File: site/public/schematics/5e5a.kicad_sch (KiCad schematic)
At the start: 60 parts, among them T2 ~4.3k:8

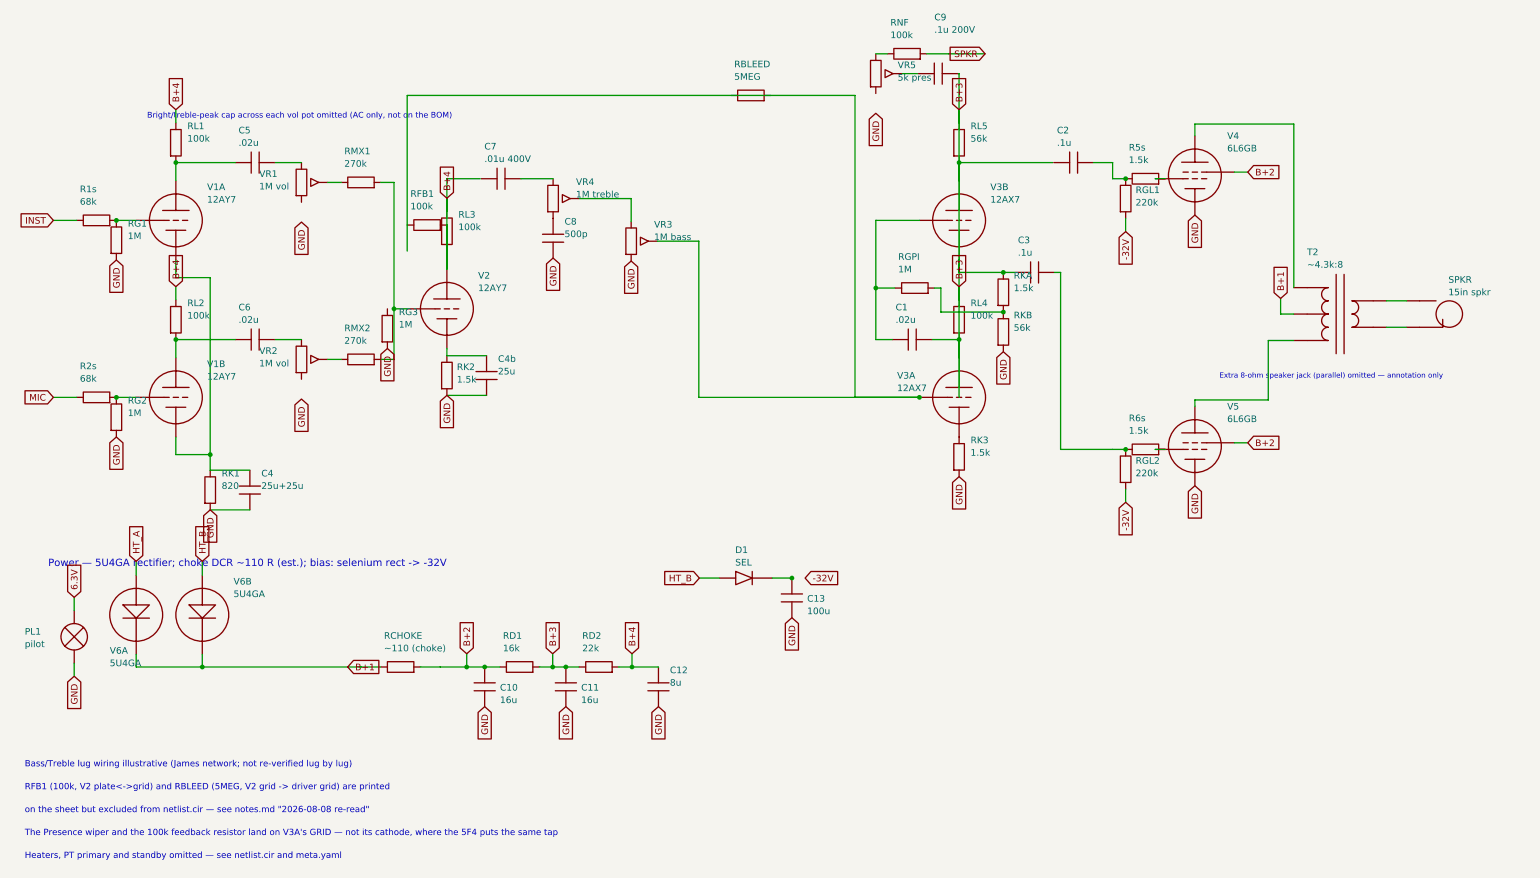
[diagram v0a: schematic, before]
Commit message: Fix: site copies of 29 sheets re-synced; regenerate step syncs before the drift check
- the drawing scripts write amps/; site/public/schematics is refreshed by
  site/scripts/sync-assets.mjs, which CI only ran inside the site build, so
  the fixer commits carried stale copies and the new drift gate caught them
- CI now syncs immediately after regenerating and diffs both trees; the
  AGENTS.md regenerate command does the same

Co-Authored-By: Claude Fable 5.1 <noreply@anthropic.com>
Claude-Session: https://claude.ai/code/session_01KBMfdh37HmCL2iWcBiL5J1
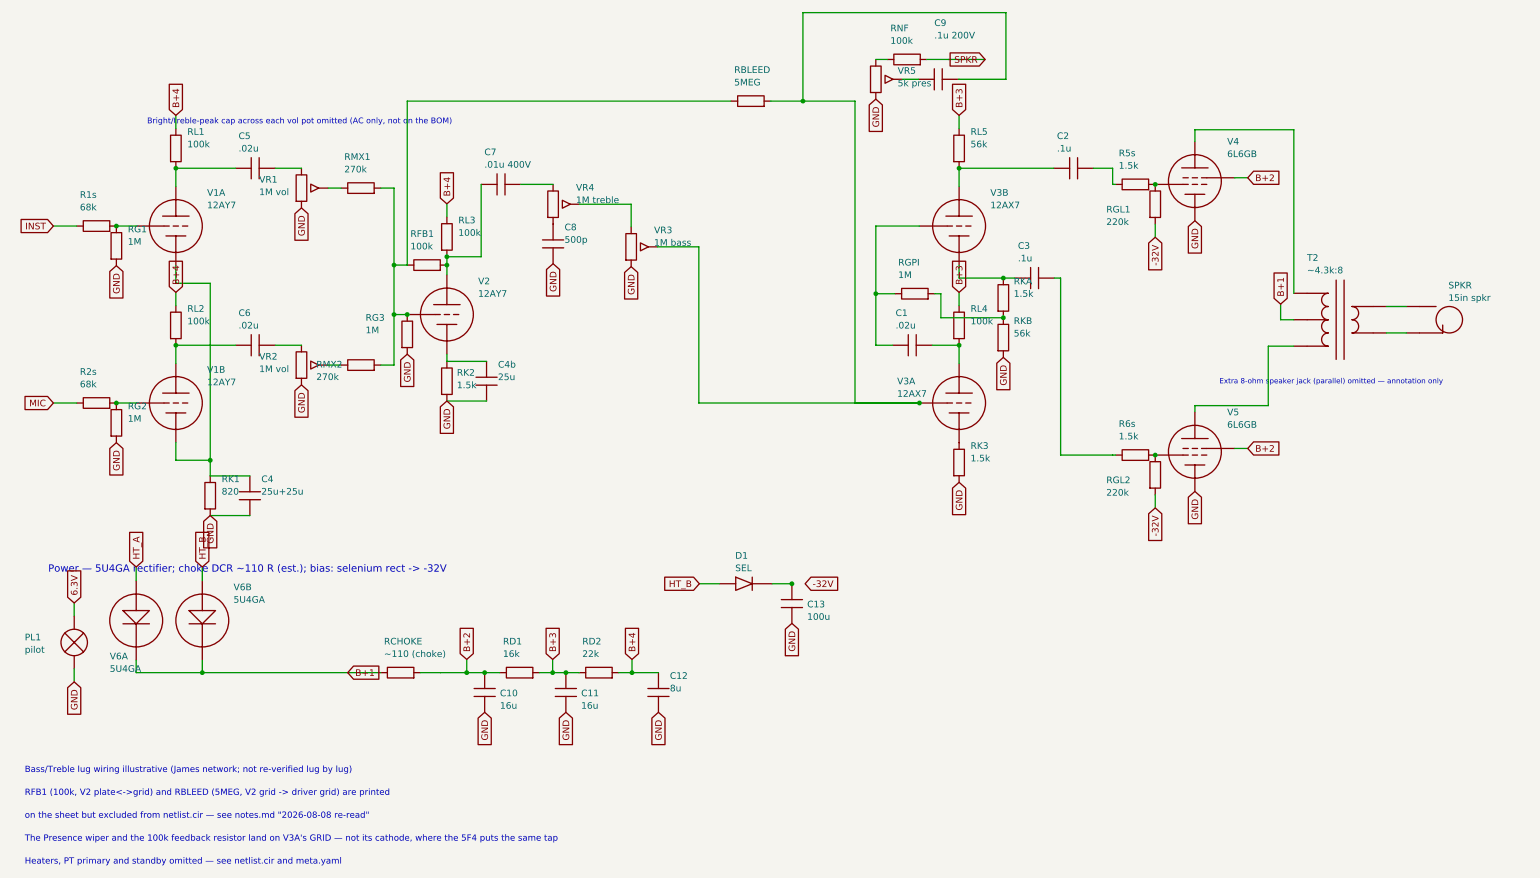
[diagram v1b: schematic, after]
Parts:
- removed C8: 500p, symbol cx:C
- removed RCHOKE: ~110 (choke), symbol cx:R
- removed RGL1, RGL2: 220k, symbol cx:R
- removed RK1: 820, symbol cx:R
- removed RK2, RK3, RKA: 1.5k, symbol cx:R
- removed SPKR: 15in spkr, symbol cx:JACK
- removed V4: 6L6GB, symbol cx:PENTODE
- removed V6B: 5U4GA, symbol cx:DIODE_TUBE
- added C1: .02u, symbol cx:C
- added C2, C3: .1u, symbol cx:C
- added C4: 25u+25u, symbol cx:C
- added C4b: 25u, symbol cx:C
- added PL1: pilot, symbol cx:LAMP
- added RKB: 56k, symbol cx:R
- added T2: ~4.3k:8, symbol cx:OT_PP
- added V3A: 12AX7, symbol cx:TRIODE
- added V6A: 5U4GA, symbol cx:DIODE_TUBE
- added VR4: 1M treble, symbol cx:POT
- C8: renamed from VR4; value 1M treble -> 500p; symbol cx:POT -> cx:C
- RCHOKE: renamed from V6A; value 5U4GA -> ~110 (choke); symbol cx:DIODE_TUBE -> cx:R
- RGL1: renamed from C2; value .1u -> 220k; symbol cx:C -> cx:R
- RGL2: renamed from C3; value .1u -> 220k; symbol cx:C -> cx:R
- RGPI: renamed from C1; value .02u -> 1M; symbol cx:C -> cx:R
- RK1: renamed from C4; value 25u+25u -> 820; symbol cx:C -> cx:R
- RK2: renamed from C4b; value 25u -> 1.5k; symbol cx:C -> cx:R
- RK3: renamed from RL4; value 100k -> 1.5k
- RKA: renamed from RGPI; value 1M -> 1.5k
- RL4: renamed from V3A; value 12AX7 -> 100k; symbol cx:TRIODE -> cx:R
- SPKR: renamed from T2; value ~4.3k:8 -> 15in spkr; symbol cx:OT_PP -> cx:JACK
- V4: renamed from RKB; value 56k -> 6L6GB; symbol cx:R -> cx:PENTODE
- V6B: renamed from PL1; value pilot -> 5U4GA; symbol cx:LAMP -> cx:DIODE_TUBE
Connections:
- net -32V: now also RGL1.2, RGL2.2
- net 6.3V: now also PL1.1; no longer V6B.1
- net B+1: now also RCHOKE.1, V6B.2 (K), T2.2 (CT), V6A.2 (K); no longer RCHOKE.2 (K)
- net B+2: now also RCHOKE.2, V4.3 (G2)
- net B+3: no longer C9.2, RGL2.1, RGPI.2, RK3.1, RK3.2, RL5.2, V3B.1 (P), V3B.3 (K)
- net B+4: no longer RFB1.2, RL3.2, V2.1 (P)
- net GND: now also C8.2, RK3.2, V4.4 (K), VR1.3, VR2.3, VR5.3, C4.2, C4b.2, PL1.2, RKB.2; no longer V4.2, V6B.2
- net HT_A: now also V6A.1 (A); no longer RCHOKE.1 (A)
- net HT_B: now also V6B.1 (A)
- net at C7.1: now also RFB1.2, RL3.2, V2.1 (P)
- net at C7.2: now also VR4.1; no longer C8.1
- net at V4.1 (P): now also T2.1 (PRI_A); no longer RKA.2
- net at RGL1.1: now also R5s.2, V4.2 (G1)
- net at R5s.1: now also C2.2; no longer RGL1.2
- net at V5.1 (P): now also T2.3 (PRI_B)
- net at R6s.2, V5.2 (G1): now also RGL2.1
- net at R6s.1: now also C3.2; no longer RGL2.2
- net at RK2.1, V2.3 (K): now also C4b.1
- net at RMX1.2, RMX2.2, V2.2 (G): now also RBLEED.1, RFB1.1, RG3.1
- net at RK1.1, V1A.3 (K), V1B.3 (K): now also C4.1
- net at RGPI.1, V3B.2 (G): now also C1.1; no longer RKA.1
- net at SPKR.1 (T): now also T2.4 (SEC_H)
- net at SPKR.2 (S): now also T2.5 (SEC_C)
- net at VR5.2 (W): now also C9.1
- net at VR3.1: now also VR4.2 (W); no longer C8.2 (W)
- new net: C2.1, RL5.2, V3B.1 (P)
- new net: C3.1, RKA.1, V3B.3 (K)
- new net: C1.2, RL4.2, V3A.1 (P)
- new net: C9.2, RBLEED.2, V3A.2 (G), VR3.2 (W)
- new net: C8.1, VR4.3
- new net: RK3.1, V3A.3 (K)
- new net: RGPI.2, RKA.2, RKB.1
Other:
- moved on the sheet: C5, R1s, RFB1, RG1, RK3, RKA, RL1, RMX1, V1A, VR1
